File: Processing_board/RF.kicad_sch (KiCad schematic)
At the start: 13 parts, among them J22 CONMHF1-SMD-G-T, U15 BGS13SN8E6327XTSA1

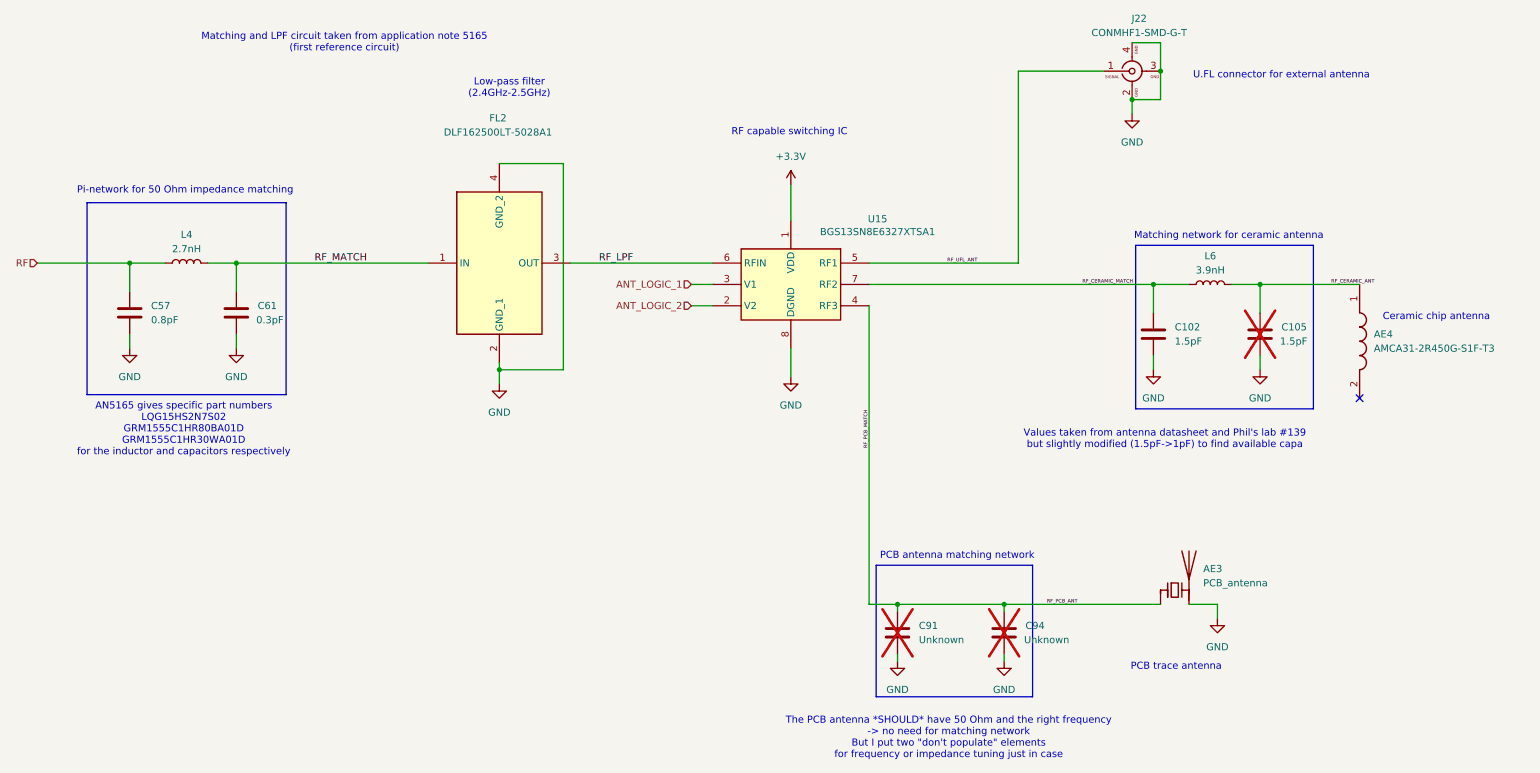
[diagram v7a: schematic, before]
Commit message: had to rename all components on the PCB to match the schematic
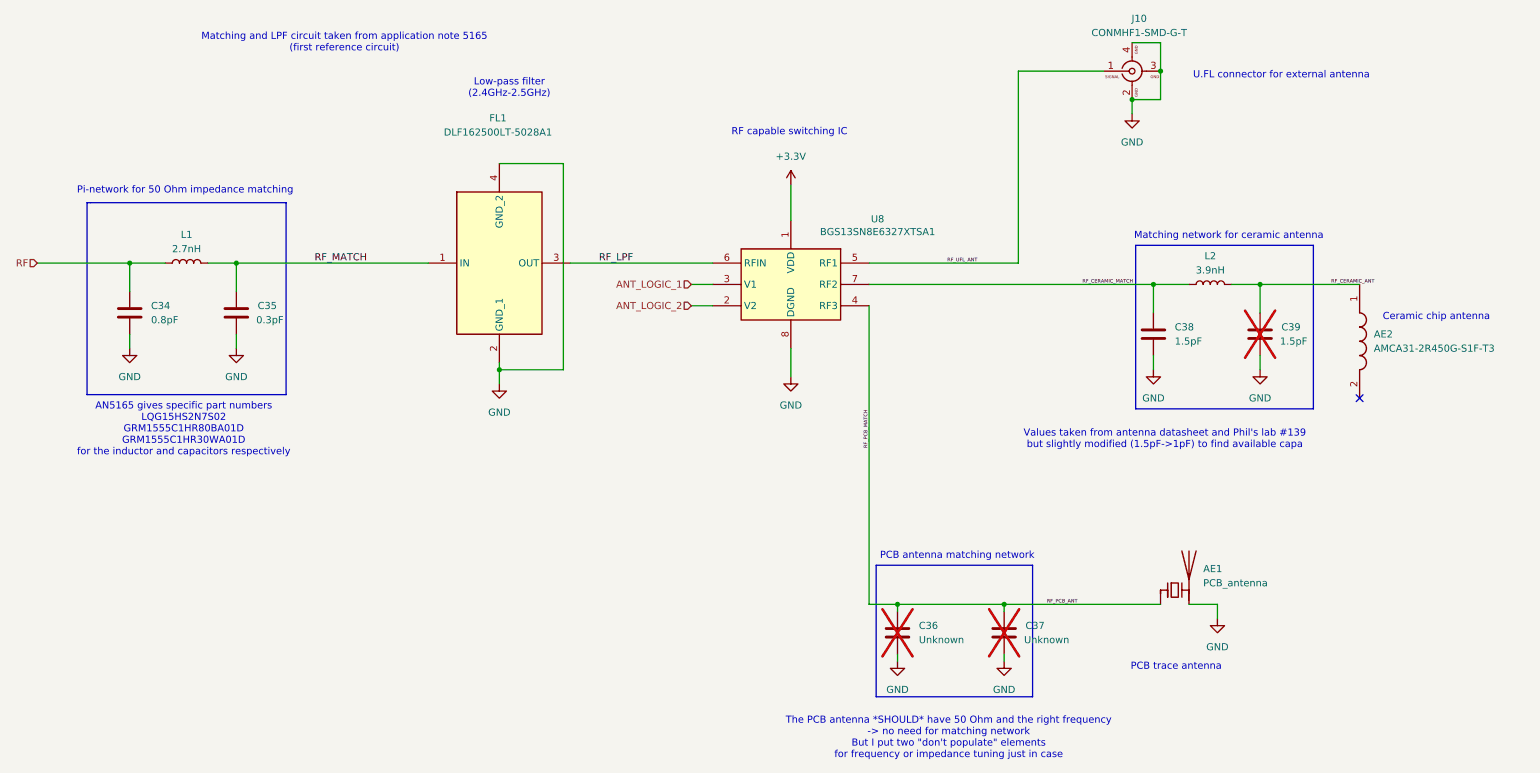
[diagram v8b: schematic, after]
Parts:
- renumbered AE3 to AE1, AE4 to AE2, C57 to C34, C61 to C35, C91 to C36, C94 to C37, C102 to C38, C105 to C39, FL2 to FL1, J22 to J10, L4 to L1, L6 to L2, U15 to U8
